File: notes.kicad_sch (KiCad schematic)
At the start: 0 parts

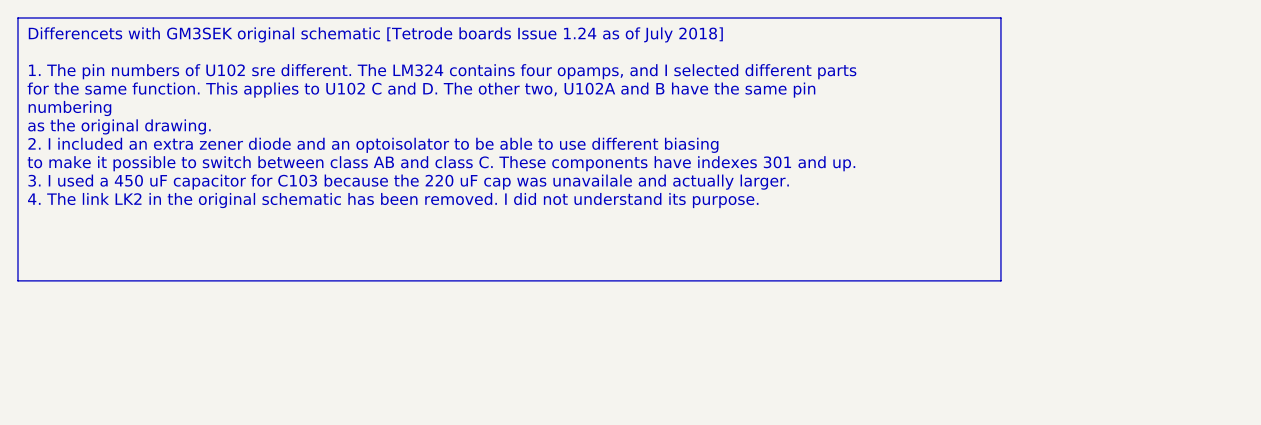
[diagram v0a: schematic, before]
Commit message: Updated format to KiCad 9. Included footprints etc.
Standardized PCB layers, updated property formatting, and adjusted net assignments. Added some DigiKey, Electrokit, and Mouser component part numbers.
Reduced font sizes for better readability and incorporated embedded font settings.
Removed the sequencer from the schematic which wasn't really meant to be there.
Revised and excluded drc and erc warnings and exclusions.
Included footprints into the project library that formerly was defined outside of the project.
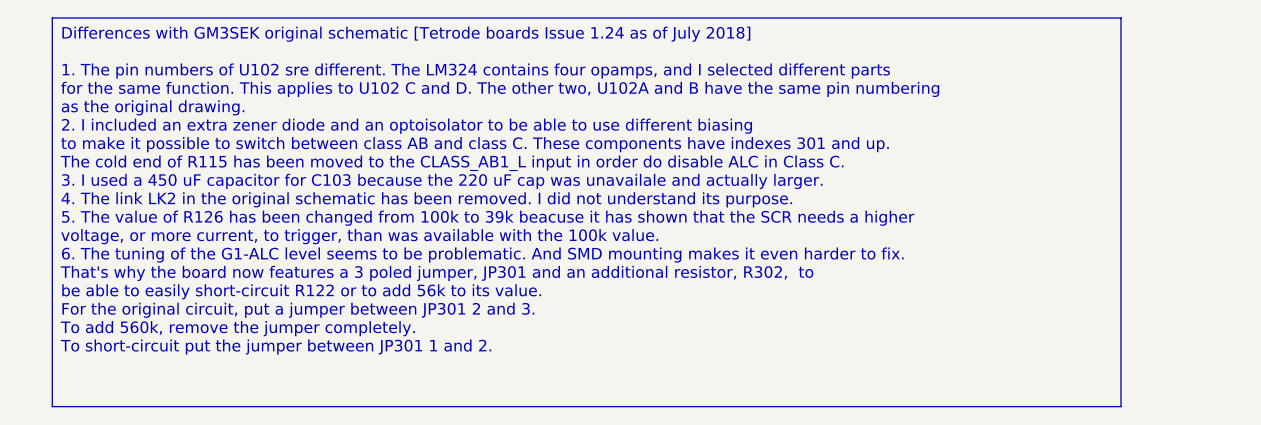
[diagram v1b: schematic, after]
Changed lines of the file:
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@@
 (kicad_sch
-	(version 20231120)
+	(version 20250114)
 	(generator "eeschema")
-	(generator_version "8.0")
+	(generator_version "9.0")
 	(paper "A4")
-	(text_box "Differencets with GM3SEK original schematic [Tetrode boards Issue 1.24 as of July 2018]\n\n1. The pin numbers of U102 sre different. The LM324 contains four opamps, and I selected different parts \n    for the same function. This applies to U102 C and D. The other two, U102A and B have the same pin numbering \nas the original drawing.\n2. I included an extra zener diode and an optoisolator to be able to use different biasing\n   to make it possible to switch between class AB and class C. These components have indexes 301 and up.\n3. I used a 450 uF capacitor for C103 because the 220 uF cap was unavailale and actually larger.\n4. The link LK2 in the original schematic has been removed. I did not understand its purpose.\n"
+	(text_box "Differences with GM3SEK original schematic [Tetrode boards Issue 1.24 as of July 2018]\n\n1. The pin numbers of U102 sre different. The LM324 contains four opamps, and I selected different parts \n    for the same function. This applies to U102 C and D. The other two, U102A and B have the same pin numbering \nas the original drawing.\n2. I included an extra zener diode and an optoisolator to be able to use different biasing\n   to make it possible to switch between class AB and class C. These components have indexes 301 and up.\n   The cold end of R115 has been moved to the CLASS_AB1_L input in order do disable ALC in Class C.\n3. I used a 450 uF capacitor for C103 because the 220 uF cap was unavailale and actually larger.\n4. The link LK2 in the original schematic has been removed. I did not understand its purpose.\n5. The value of R126 has been changed from 100k to 39k beacuse it has shown that the SCR needs a higher\n   voltage, or more current, to trigger, than was available with the 100k value.\n6. The tuning of the G1-ALC level seems to be problematic. And SMD mounting makes it even harder to fix.\n   That's why the board now features a 3 poled jumper, JP301 and an additional resistor, R302,  to\n   be able to easily short-circuit R122 or to add 56k to its value. \n   For the original circuit, put a jumper between JP301 2 and 3.\n   To add 560k, remove the jumper completely. \n   To short-circuit put the jumper between JP301 1 and 2.\n"
 		(exclude_from_sim no)
-		(at 19.05 22.86 0)
-		(size 109.22 29.21)
+		(at 22.86 22.86 0)
+		(size 118.745 43.18)
+		(margins 0.9525 0.9525 0.9525 0.9525)
 		(stroke
 			(width 0)
